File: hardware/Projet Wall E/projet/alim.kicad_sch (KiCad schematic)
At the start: 34 parts, among them J1 Conn_01x02_Pin, J2 USB_C_Receptacle_USB2.0_16P, U1 BQ25895RTW, U2 AP2112K-3.3, U3 BQ27441DRZR-G1A

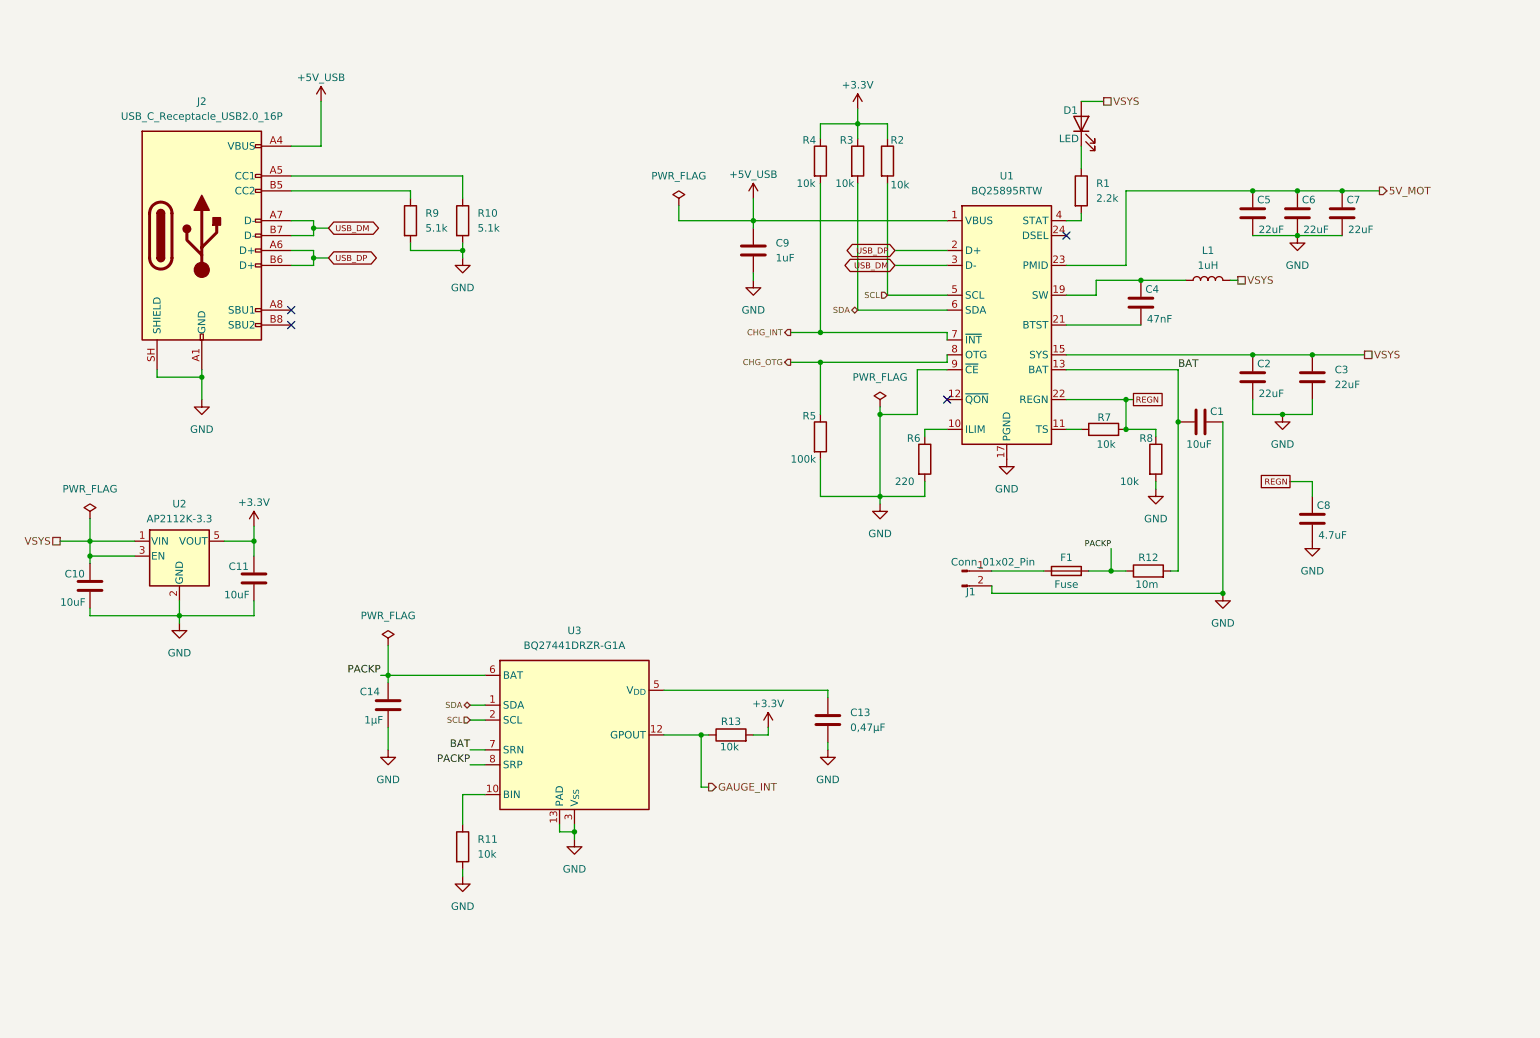
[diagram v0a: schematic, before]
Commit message: Alim : BQ25896 + BQ27220, symboles perso wall_e, USB vers MCU
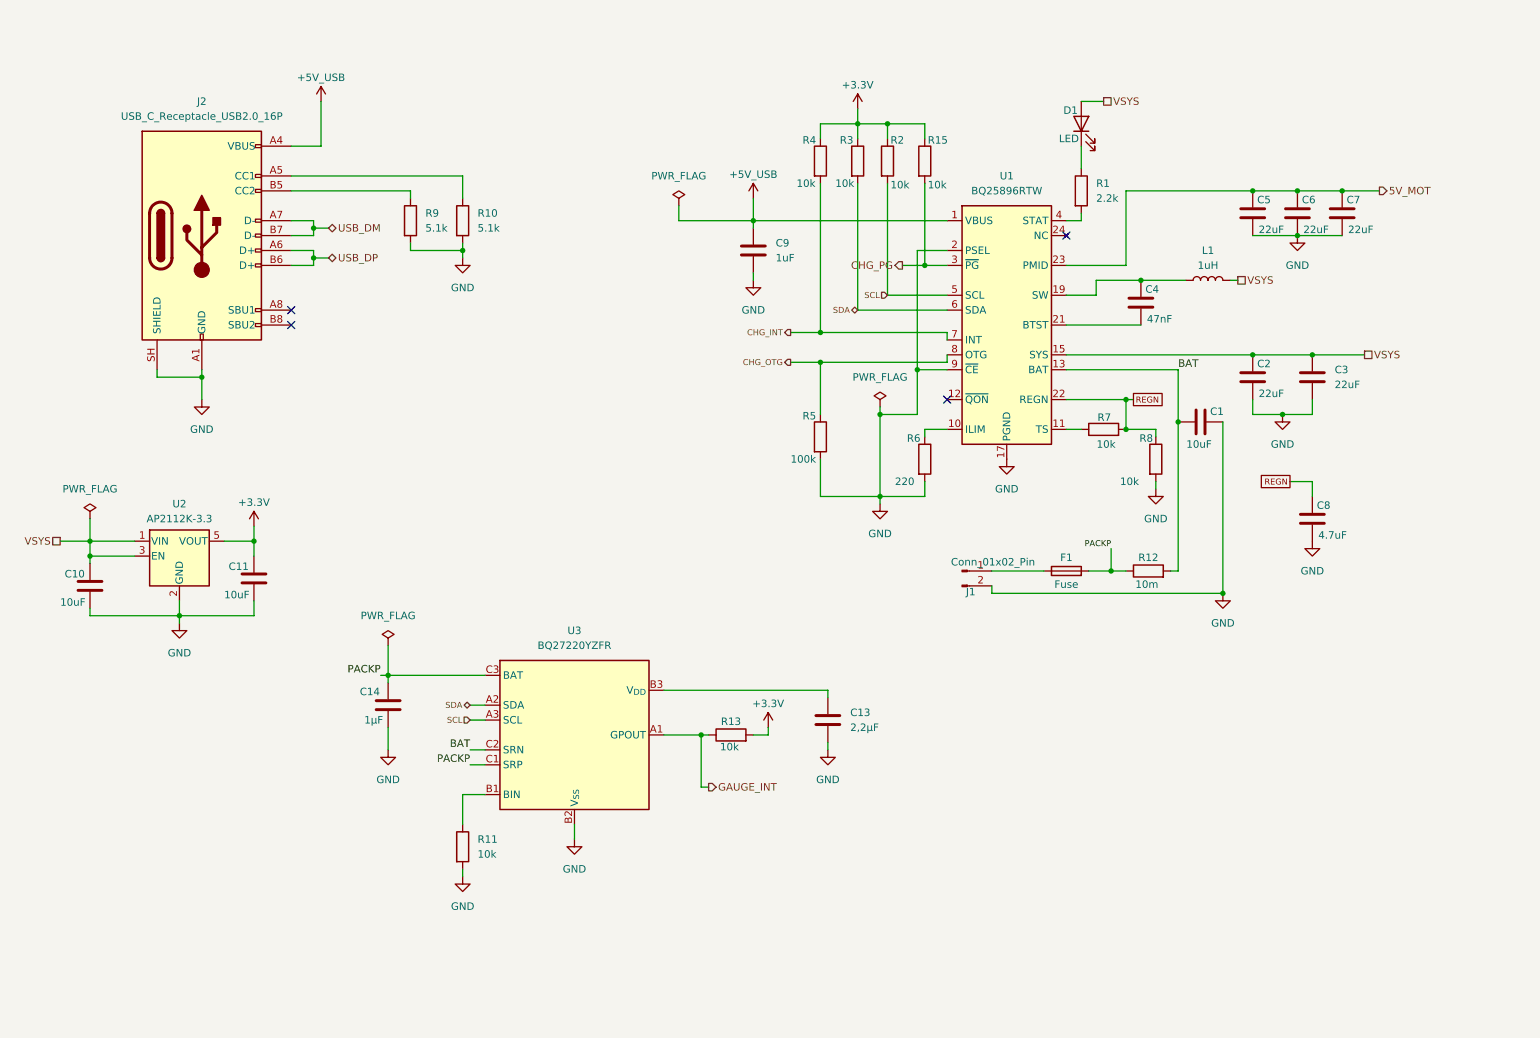
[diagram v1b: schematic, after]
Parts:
- removed U1: BQ25895RTW, Package_DFN_QFN:Texas_RTW_WQFN-24-1EP_4x4mm_P0.5mm_EP2.7x2.7mm_ThermalVias, symbol wall_e:BQ25895RTW
- removed U3: BQ27441DRZR-G1A, Package_SON:Texas_S-PDSO-N12, symbol wall_e:BQ27441DRZR-G1A
- added R15: 10k, Resistor_SMD:R_01005_0402Metric, symbol wall_e:R
- added U1: BQ25896RTW, Package_DFN_QFN:Texas_RTW_WQFN-24-1EP_4x4mm_P0.5mm_EP2.7x2.7mm_ThermalVias, symbol wall_e:BQ25896RTW
- added U3: BQ27220YZFR, Package_BGA:Texas_DSBGA-9_1.62x1.58mm_Layout3x3_P0.5mm, symbol wall_e:BQ27220YZFR
- C13: value 0,47µF -> 2,2µF
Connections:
- net +3.3V: now also R15.1
- net +5V_USB: now also U1.1 (VBUS)
- net 5V_MOT: now also U1.23 (PMID)
- net BAT: now also U1.13 (BAT), U1.14 (BAT), U3.C2 (SRN)
- net CHG_INT: now also U1.7 (INT)
- net CHG_OTG: now also U1.8 (OTG)
- net GAUGE_INT: now also U3.A1 (GPOUT)
- net GND: now also U1.17 (PGND), U1.18 (PGND), U1.2 (PSEL), U1.25 (PGND), U1.9 (~{CE}), U3.B2 (V_{SS})
- net PACKP: now also U3.C1 (SRP), U3.C3 (BAT)
- net REGN: now also U1.22 (REGN)
- net SCL: now also U1.5 (SCL), U3.A3 (SCL)
- net SDA: now also U1.6 (SDA), U3.A2 (SDA)
- net VSYS: now also U1.15 (SYS), U1.16 (SYS)
- net at R1.2: now also U1.4 (STAT)
- net at R6.1: now also U1.10 (ILIM)
- net at R7.1: now also U1.11 (TS)
- net at C13.1: now also U3.B3 (V_{DD})
- net at R11.1: now also U3.B1 (BIN)
- net at C4.1: now also U1.21 (BTST)
- net at C4.2, L1.1: now also U1.19 (SW), U1.20 (SW)
- new net CHG_PG: R15.2, U1.3 (~{PG})

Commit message: Alim : BQ25896 + BQ27220, diode idéale, USB vers MCU
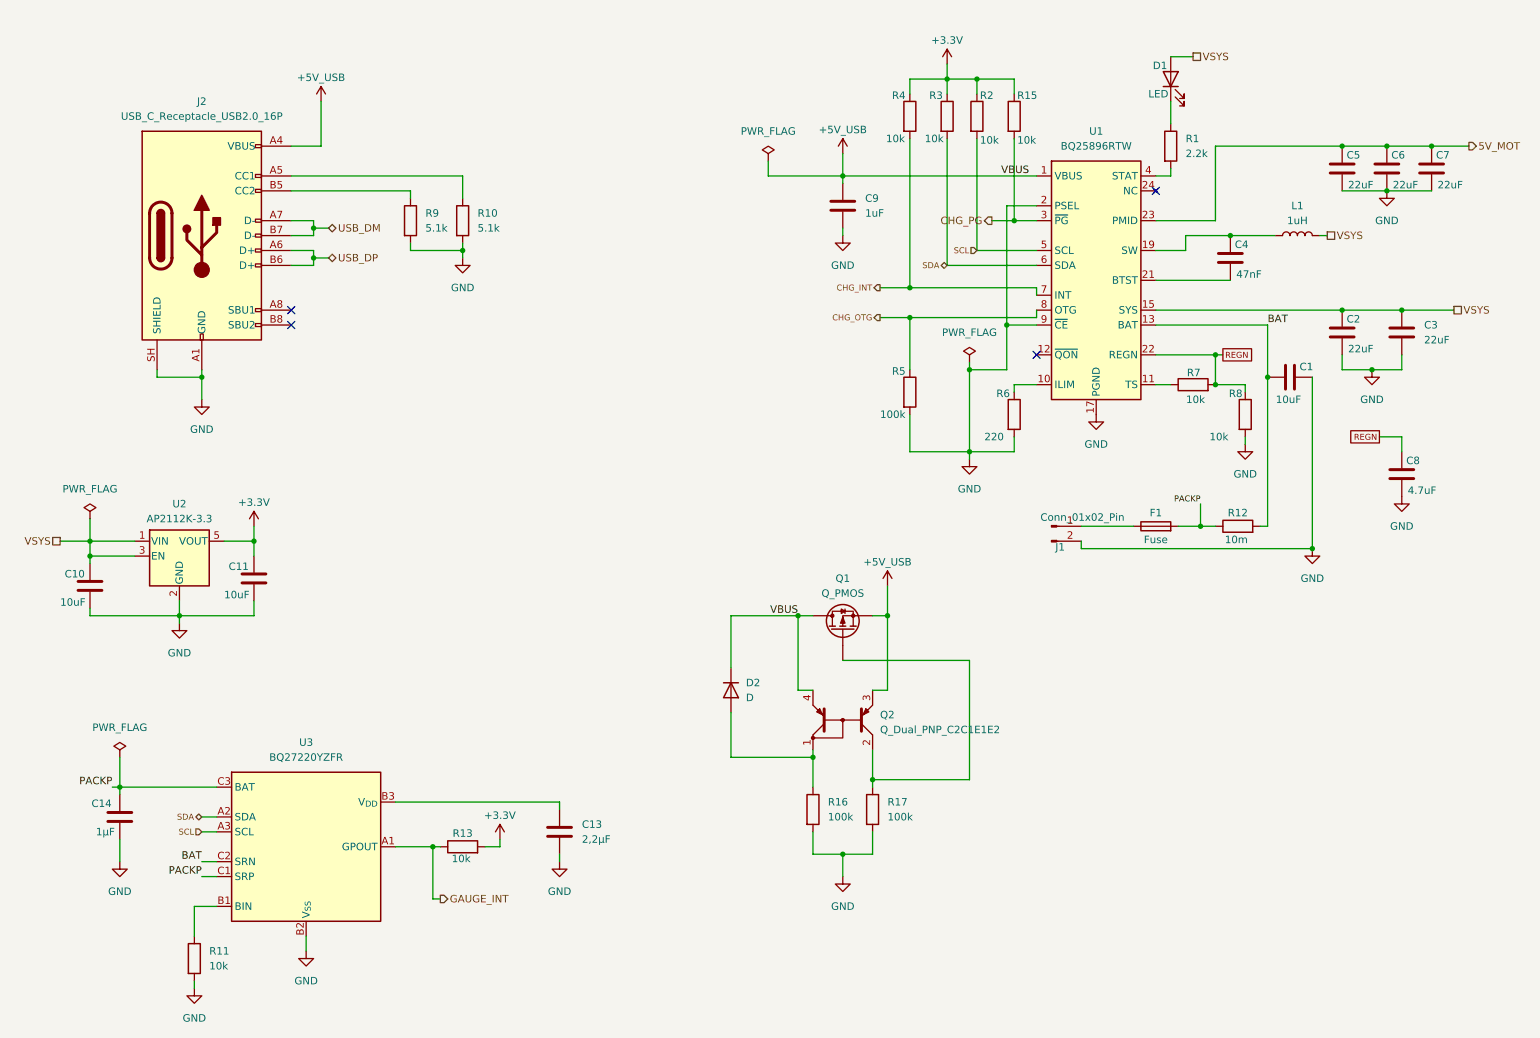
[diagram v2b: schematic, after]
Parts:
- added D2: D, Diode_SMD:D_SOD-523, symbol Device:D
- added Q1: Q_PMOS, Package_TO_SOT_SMD:SOT-23-3, symbol Device:Q_PMOS
- added Q2: Q_Dual_PNP_C2C1E1E2, Package_TO_SOT_SMD:SOT-363_SC-70-6, symbol Transistor_BJT:Q_Dual_PNP_C2C1E1E2
- added R16, R17: 100k, Resistor_SMD:R_0402_1005Metric, symbol wall_e:R
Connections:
- net +5V_USB: now also D2.1 (K), Q1.D, Q1.S, Q2.3 (E1), Q2.4 (E2)
- net GND: now also R16.2, R17.2
- new net: Q1.G, Q2.2 (C1), R17.1
- new net: D2.2 (A), Q2.1 (C2), R16.1
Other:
- moved on the sheet: C1, C13, C14, C2, C3, C4, C5, C6, C7, C8, C9, D1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

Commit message: Schéma alim : TVS D4, diode idéale +5V_USB, PWR_FLAG
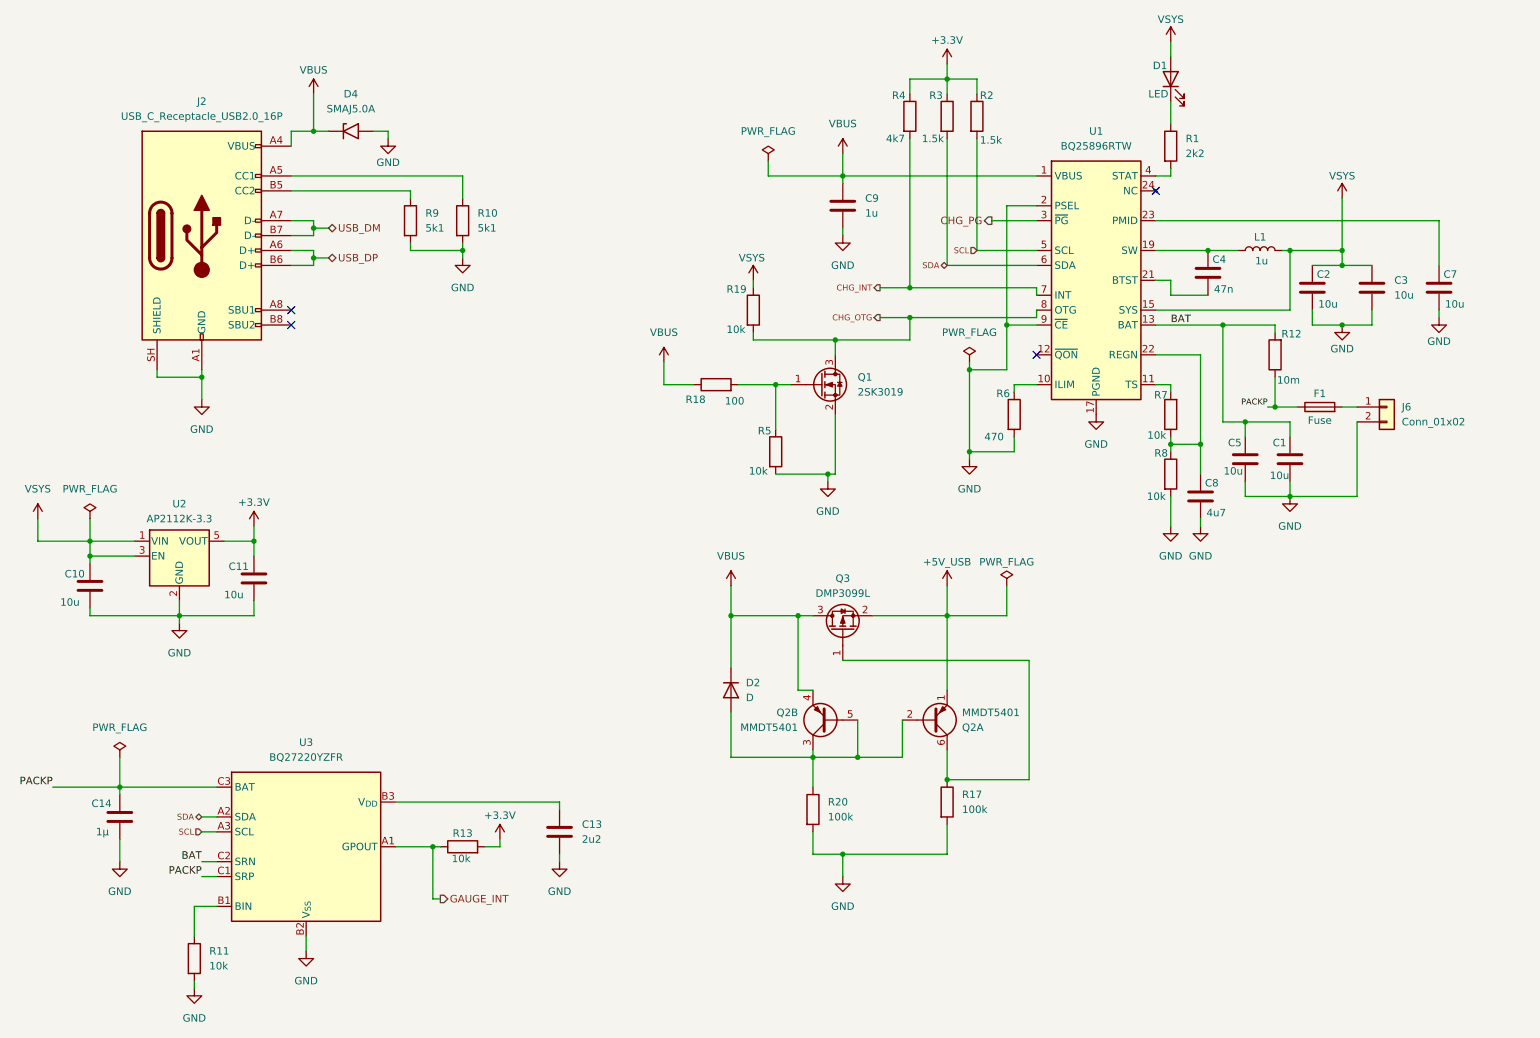
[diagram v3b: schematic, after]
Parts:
- removed C6: 22uF, Capacitor_SMD:C_0402_1005Metric, symbol wall_e:C
- removed J1: Conn_01x02_Pin, Connector_JST:JST_PH_S2B-PH-K_1x02_P2.00mm_Horizontal, symbol wall_e:Conn_01x02_Pin
- removed Q1: Q_PMOS, Package_TO_SOT_SMD:SOT-23-3, symbol Device:Q_PMOS
- removed Q2: Q_Dual_PNP_C2C1E1E2, Package_TO_SOT_SMD:SOT-363_SC-70-6, symbol Transistor_BJT:Q_Dual_PNP_C2C1E1E2
- removed R15: 10k, Resistor_SMD:R_01005_0402Metric, symbol wall_e:R
- added D4: SMAJ5.0A, Diode_SMD:D_SMA, symbol Diode:SMAJ5.0A
- added J6: Conn_01x02, Connector_JST:JST_PH_S2B-PH-K_1x02_P2.00mm_Horizontal, symbol Connector_Generic:Conn_01x02
- added Q1: 2SK3019, Package_TO_SOT_SMD:SOT-523, symbol Transistor_FET:2SK3019
- added Q2: MMDT5401, Package_TO_SOT_SMD:SOT-363_SC-70-6, symbol Transistor_BJT:MMDT5401
- added Q3: DMP3099L, Package_TO_SOT_SMD:SOT-23, symbol Transistor_FET:DMP3099L
- added R18: 100, Resistor_SMD:R_01005_0402Metric, symbol wall_e:R
- added R19: 10k, Resistor_SMD:R_01005_0402Metric, symbol wall_e:R
- C1, C10, C11: value 10uF -> 10u
- C13: value 2,2µF -> 2u2
- C14: value 1µF -> 1µ
- C2, C3, C5, C7: value 22uF -> 10u
- C4: value 47nF -> 47n
- C8: value 4.7uF -> 4u7
- C9: value 1uF -> 1u
- L1: value 1uH -> 1u
- R1: value 2.2k -> 2k2
- R10, R9: value 5.1k -> 5k1
- R2, R3: value 10k -> 1.5k
- R4: value 10k -> 4k7
- R5: value 100k -> 10k
- R6: value 220 -> 470
- renumbered R16 to R20
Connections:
- net +5V_USB: now also Q2.1 (E1), Q3.2 (S); no longer C9.1, D2.1 (K), J2.A4 (VBUS), J2.A9 (VBUS), J2.B4 (VBUS), J2.B9 (VBUS), U1.1 (VBUS)
- net BAT: now also C1.2, C5.2; no longer C1.1
- net CHG_OTG: now also Q1.3 (D), R19.2; no longer R5.1
- net GND: now also C1.1, D4.2 (A2), J6.2 (Pin_2), Q1.2 (S); no longer C1.2
- net PACKP: now also F1.1; no longer F1.2
- net VSYS: now also R19.1
- net at R17.1: now also Q2.6 (C1), Q3.1 (G)
- net at R7.1: now also C8.2, R8.1, U1.22 (REGN); no longer U1.11 (TS)
- net at D2.2 (A), R20.1: now also Q2.2 (B1), Q2.3 (C2), Q2.5 (B2)
- net 5V_MOT: no longer names the net of C7.2, U1.23 (PMID)
- net 5V_MOT: no longer C5.2
- removed net REGN: C8.2, R7.2, R8.1, U1.22 (REGN)
- new net: Q1.1 (G), R18.2, R5.1
- new net: R7.2, U1.11 (TS)
- new net: F1.2, J6.1 (Pin_1)
- new net VBUS: C9.1, D2.1 (K), D4.1 (A1), J2.A4 (VBUS), J2.A9 (VBUS), J2.B4 (VBUS), J2.B9 (VBUS), Q2.4 (E2), Q3.3 (D), R18.1, U1.1 (VBUS)
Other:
- moved on the sheet: C1, C2, C3, C4, C7, C8, L1, R12, R17, R5, R7, R8

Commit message: Add files via upload
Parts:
- removed D4: SMAJ5.0A, Diode_SMD:D_SMA, symbol Diode:SMAJ5.0A
- added U6: USBLC6-2SC6, Package_TO_SOT_SMD:SOT-23-6, symbol Power_Protection:USBLC6-2SC6
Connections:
- net GND: now also U6.2 (GND)
- net USB_DM: now also U6.6 (I/O1); no longer J2.A7 (D-), J2.B7 (D-)
- net USB_DP: now also U6.4 (I/O2); no longer J2.A6 (D+), J2.B6 (D+)
- net VBUS: now also U6.5 (VBUS)
- new net: J2.A7 (D-), J2.B7 (D-), U6.1 (I/O1)
- new net: J2.A6 (D+), J2.B6 (D+), U6.3 (I/O2)

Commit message: Alim : refs JLCPCB, correction empreintes, renommage R30-R32
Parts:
- C1, C2, C3, C5, C7: footprint Capacitor_SMD:C_0402_1005Metric -> Capacitor_SMD:C_0603_1608Metric; JLCPCB Parts (none) -> C19702
- C10, C11: footprint Capacitor_SMD:C_0805_2012Metric -> Capacitor_SMD:C_0603_1608Metric; JLCPCB Parts (none) -> C19702
- C13: JLCPCB Parts (none) -> C12530
- C14, C9: JLCPCB Parts (none) -> C52923
- C4: JLCPCB Parts (none) -> C307434
- C8: footprint Capacitor_SMD:C_0402_1005Metric -> Capacitor_SMD:C_0603_1608Metric; JLCPCB Parts (none) -> C19666
- D1: JLCPCB Parts (none) -> C2286
- D2: JLCPCB Parts (none) -> C81598
- F1: footprint Fuse:Fuse_1812_4532Metric -> Fuse:Fuse_1206_3216Metric; JLCPCB Parts (none) -> C545216
- J2: JLCPCB Parts (none) -> C165948
- J6: footprint Connector_JST:JST_PH_S2B-PH-K_1x02_P2.00mm_Horizontal -> Connector_JST:JST_PH_S2B-PH-SM4-TB_1x02-1MP_P2.00mm_Horizontal; JLCPCB Parts (none) -> C295747
- L1: footprint (none) -> Inductor_SMD:L_Sunlord_SWPA4030S; JLCPCB Parts (none) -> C435273
- Q1: JLCPCB Parts (none) -> C261283
- Q2: JLCPCB Parts (none) -> C460236
- Q3: JLCPCB Parts (none) -> C155244
- R1: JLCPCB Parts (none) -> C25879
- R10, R9: JLCPCB Parts (none) -> C25905
- R11: JLCPCB Parts (none) -> C25744
- R12: footprint Resistor_SMD:R_1206_3216Metric -> Resistor_SMD:R_0805_2012Metric; JLCPCB Parts (none) -> C98889
- R13, R5, R7, R8: footprint Resistor_SMD:R_01005_0402Metric -> Resistor_SMD:R_0402_1005Metric; JLCPCB Parts (none) -> C25744
- R2, R3: JLCPCB Parts (none) -> C25867
- R20: JLCPCB Parts (none) -> C25741
- R30: renamed from R19; footprint Resistor_SMD:R_01005_0402Metric -> Resistor_SMD:R_0402_1005Metric; JLCPCB Parts (none) -> C25744
- R31: renamed from R18; footprint Resistor_SMD:R_01005_0402Metric -> Resistor_SMD:R_0402_1005Metric; JLCPCB Parts (none) -> C25076
- R32: renamed from R17; JLCPCB Parts (none) -> C25741
- R4: JLCPCB Parts (none) -> C25900
- R6: footprint Resistor_SMD:R_01005_0402Metric -> Resistor_SMD:R_0402_1005Metric; JLCPCB Parts (none) -> C25117
- U1: JLCPCB Parts (none) -> C181475
- U2: JLCPCB Parts (none) -> C51118
- U3: JLCPCB Parts (none) -> C528617
- U6: JLCPCB Parts (none) -> C7519
